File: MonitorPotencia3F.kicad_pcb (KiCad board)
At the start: 2 copper layers, 95.9 x 97.2 mm, 42 parts, among them J1 Conn_01x02, J2 Conn_01x02, J3 Conn_01x02, J4 Conn_01x02, J5 Conn_01x02, J6 Conn_01x04, J7 Conn_01x04, J8 Conn_01x04, J9 Conn_02x09_Odd_Even, U1 LM7805, U2 ESP32-DEVKIT-V1, U3 LM324

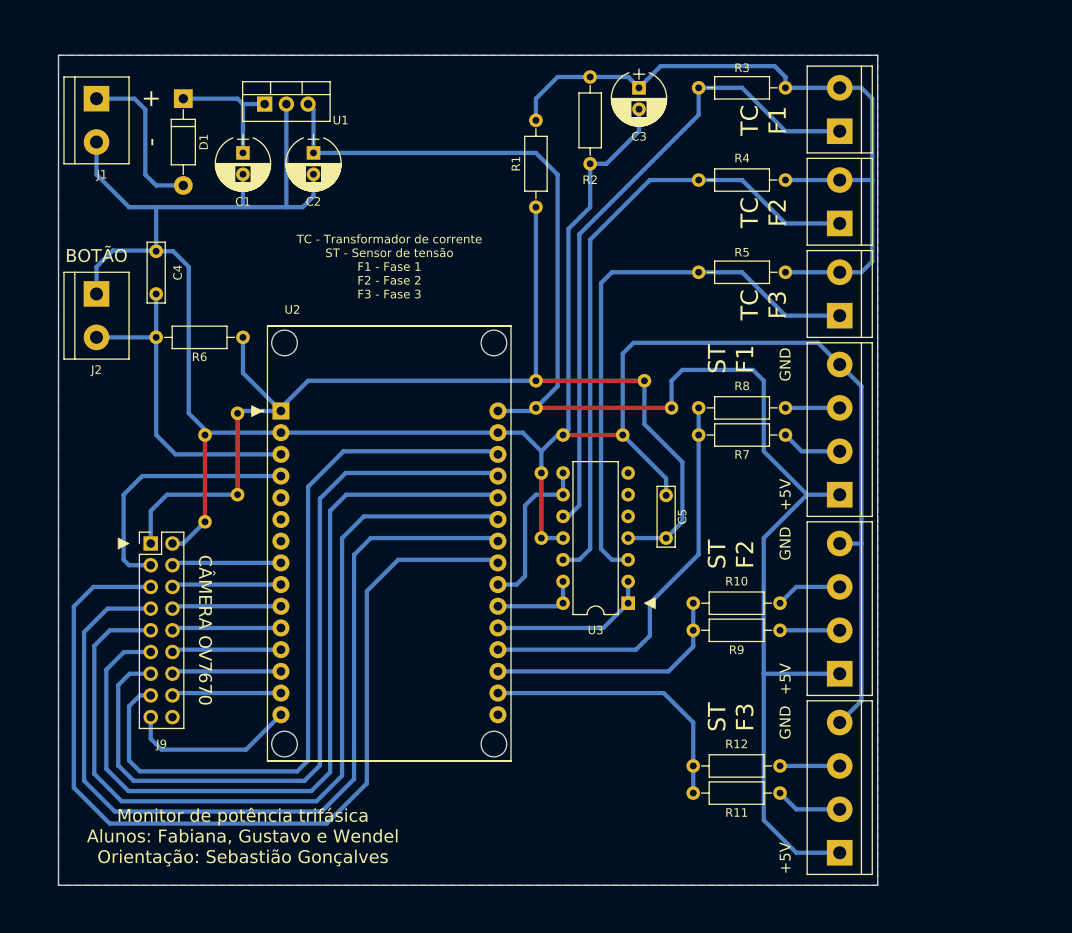
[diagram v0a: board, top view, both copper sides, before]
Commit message: PCB e modelo 3D foram completados. As alterações necessárias foram feitas no esquemático para refletir o projeto desenvolvido na PCB. Teve-se que alterar o modelo do ESP32 para aquele que foi adquirido para o projeto.
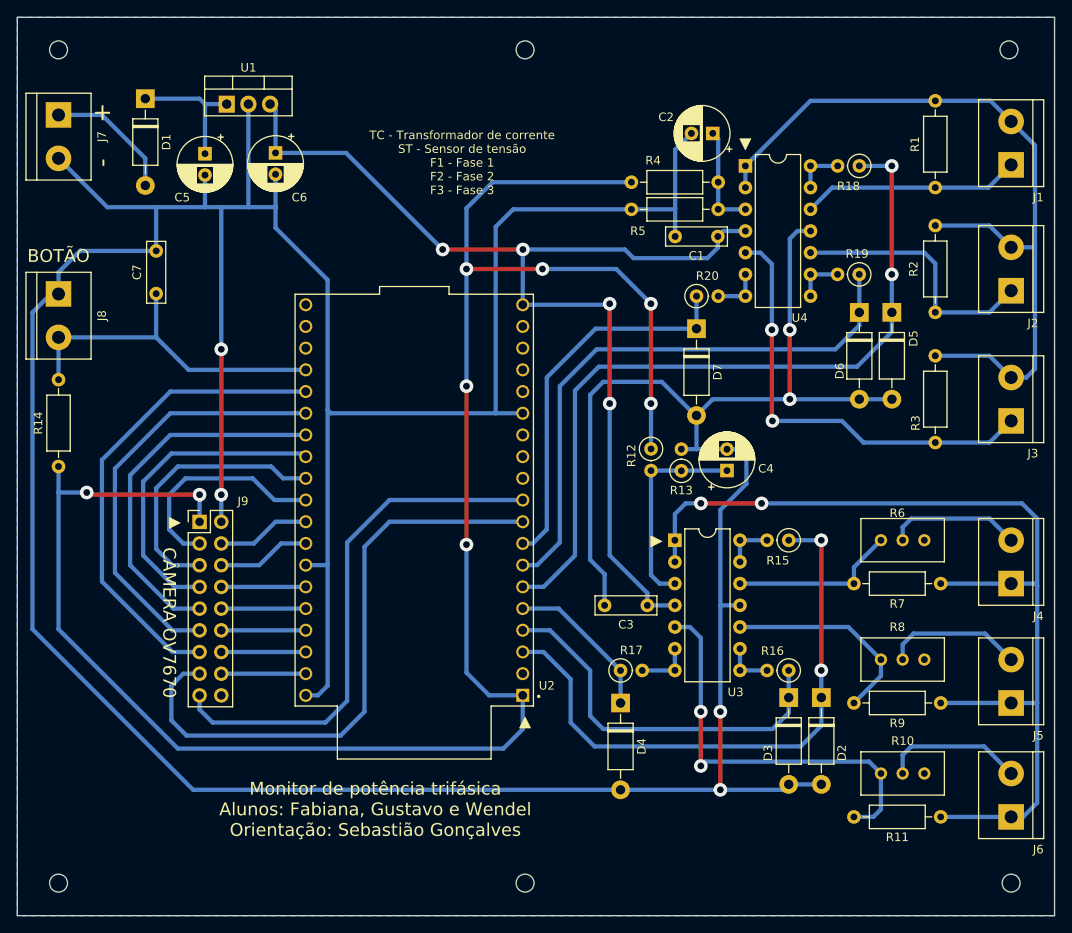
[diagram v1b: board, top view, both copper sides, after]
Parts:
- removed the REF** at (161.3, 82.5)
- removed the REF** at (122.6, 95.9)
- removed the REF** at (161.9, 90.2)
- removed the REF** at (122.6, 85.7)
- removed the REF** at (161.9, 97.8)
- removed the REF** at (161.3, 79.4)
- removed the REF** at (126.4, 92.7)
- removed the REF** at (174.0, 79.4)
- removed the REF** at (171.4, 85.7)
- removed the REF** at (177.2, 82.5)
- removed the REF** at (126.4, 83.2)
- removed the REF** at (164.5, 85.7)
- added C6: 100uF, Capacitor_THT:CP_Radial_D6.3mm_P2.50mm, F.Cu at (130.8, 52.7)
- added C7: 100nF, Capacitor_THT:C_Rect_L7.0mm_W2.0mm_P5.00mm, F.Cu at (116.8, 69.2)
- added D2: 1N4728A, Diode_THT:D_DO-41_SOD81_P10.16mm_Horizontal, F.Cu at (194.7, 116.5)
- added D3: 1N4728A, Diode_THT:D_DO-41_SOD81_P10.16mm_Horizontal, F.Cu at (190.9, 116.5)
- added D4: 1N4728A, Diode_THT:D_DO-41_SOD81_P10.16mm_Horizontal, F.Cu at (171.2, 117.1)
- added D5: 1N4728A, Diode_THT:D_DO-41_SOD81_P10.16mm_Horizontal, F.Cu at (203.0, 71.4)
- added D6: 1N4728A, Diode_THT:D_DO-41_SOD81_P10.16mm_Horizontal, F.Cu at (199.1, 71.4)
- added D7: 1N4728A, Diode_THT:D_DO-41_SOD81_P10.16mm_Horizontal, F.Cu at (180.1, 73.3)
- added R13: 10K, Resistor_THT:R_Axial_DIN0207_L6.3mm_D2.5mm_P2.54mm_Vertical, F.Cu at (178.3, 89.9)
- added R14: 4k7, Resistor_THT:R_Axial_DIN0207_L6.3mm_D2.5mm_P10.16mm_Horizontal, F.Cu at (105.4, 89.4)
- added R15: 10R, Resistor_THT:R_Axial_DIN0207_L6.3mm_D2.5mm_P2.54mm_Vertical, F.Cu at (190.9, 98.0)
- added R16: 10R, Resistor_THT:R_Axial_DIN0207_L6.3mm_D2.5mm_P2.54mm_Vertical, F.Cu at (190.9, 113.3)
- added R17: 10R, Resistor_THT:R_Axial_DIN0207_L6.3mm_D2.5mm_P2.54mm_Vertical, F.Cu at (171.2, 113.3)
- added R18: 10R, Resistor_THT:R_Axial_DIN0207_L6.3mm_D2.5mm_P2.54mm_Vertical, F.Cu at (199.1, 54.2)
- added R19: 10R, Resistor_THT:R_Axial_DIN0207_L6.3mm_D2.5mm_P2.54mm_Vertical, F.Cu at (199.1, 66.9)
- added R20: 10R, Resistor_THT:R_Axial_DIN0207_L6.3mm_D2.5mm_P2.54mm_Vertical, F.Cu at (180.1, 69.5)
- added REF**: MountingHole_2.1mm, MountingHole:MountingHole_2.1mm, F.Cu at (160.0, 40.6)
- added REF**: MountingHole_2.1mm, MountingHole:MountingHole_2.1mm, F.Cu at (160.0, 138.2)
- added REF**: MountingHole_2.1mm, MountingHole:MountingHole_2.1mm, F.Cu at (105.4, 40.6)
- added REF**: MountingHole_2.1mm, MountingHole:MountingHole_2.1mm, F.Cu at (216.9, 138.2)
- added REF**: MountingHole_2.1mm, MountingHole:MountingHole_2.1mm, F.Cu at (105.4, 138.2)
- added REF**: MountingHole_2.1mm, MountingHole:MountingHole_2.1mm, F.Cu at (216.7, 40.6)
- added U4: LM324, Package_DIP:DIP-14_W7.62mm, F.Cu at (185.8, 54.2)
- C1: value 100uF -> 100nF; footprint Capacitors_THT:CP_Radial_D6.3mm_P2.50mm -> Capacitor_THT:C_Rect_L7.0mm_W2.0mm_P5.00mm
- C2: value 100uF -> 1uF; footprint Capacitors_THT:CP_Radial_D6.3mm_P2.50mm -> Capacitor_THT:CP_Radial_D6.3mm_P2.50mm
- C3: value 1uF -> 100nF; footprint Capacitors_THT:CP_Radial_D6.3mm_P2.50mm -> Capacitor_THT:C_Rect_L7.0mm_W2.0mm_P5.00mm
- C4: value 100nF -> 1uF; footprint Capacitors_THT:C_Rect_L7.0mm_W2.0mm_P5.00mm -> Capacitor_THT:CP_Radial_D6.3mm_P2.50mm
- C5: value 100nF -> 100uF; footprint Capacitors_THT:C_Rect_L7.0mm_W2.0mm_P5.00mm -> Capacitor_THT:CP_Radial_D6.3mm_P2.50mm
- D1: footprint Diodes_THT:D_DO-41_SOD81_P10.16mm_Horizontal -> Diode_THT:D_DO-41_SOD81_P10.16mm_Horizontal
- J1, J2, J3, J4, J5: footprint Connectors_Terminal_Blocks:TerminalBlock_bornier-2_P5.08mm -> TerminalBlock:TerminalBlock_bornier-2_P5.08mm
- J6, J7, J8: value Conn_01x04 -> Conn_01x02; footprint Connectors_Terminal_Blocks:TerminalBlock_bornier-4_P5.08mm -> TerminalBlock:TerminalBlock_bornier-2_P5.08mm
- J9: footprint Pin_Headers:Pin_Header_Straight_2x09_Pitch2.54mm -> Connector_PinHeader_2.54mm:PinHeader_2x09_P2.54mm_Vertical
- R1, R2: value 10k -> 22; footprint Resistors_THT:R_Axial_DIN0207_L6.3mm_D2.5mm_P10.16mm_Horizontal -> Resistor_THT:R_Axial_DIN0207_L6.3mm_D2.5mm_P10.16mm_Horizontal
- R10, R8: value 10k -> 100k; footprint Resistors_THT:R_Axial_DIN0207_L6.3mm_D2.5mm_P10.16mm_Horizontal -> Potentiometer_THT:Potentiometer_Bourns_3296W_Vertical
- R11, R7, R9: value 1k -> 10k; footprint Resistors_THT:R_Axial_DIN0207_L6.3mm_D2.5mm_P10.16mm_Horizontal -> Resistor_THT:R_Axial_DIN0207_L6.3mm_D2.5mm_P10.16mm_Horizontal
- R12: value 10k -> 10K; footprint Resistors_THT:R_Axial_DIN0207_L6.3mm_D2.5mm_P10.16mm_Horizontal -> Resistor_THT:R_Axial_DIN0207_L6.3mm_D2.5mm_P2.54mm_Vertical
- R3: footprint Resistors_THT:R_Axial_DIN0207_L6.3mm_D2.5mm_P10.16mm_Horizontal -> Resistor_THT:R_Axial_DIN0207_L6.3mm_D2.5mm_P10.16mm_Horizontal
- R4, R5: value 22 -> 10k; footprint Resistors_THT:R_Axial_DIN0207_L6.3mm_D2.5mm_P10.16mm_Horizontal -> Resistor_THT:R_Axial_DIN0207_L6.3mm_D2.5mm_P10.16mm_Horizontal
- R6: value 4k7 -> 100k; footprint Resistors_THT:R_Axial_DIN0207_L6.3mm_D2.5mm_P10.16mm_Horizontal -> Potentiometer_THT:Potentiometer_Bourns_3296W_Vertical
- U1: footprint TO_SOT_Packages_THT:TO-220-3_Vertical -> Package_TO_SOT_THT:TO-220-3_Vertical
- U2: value ESP32-DEVKIT-V1 -> ESP32-DEVKITC; footprint ESP32-DEVKIT-V1:MODULE_ESP32_DEVKIT_V1 -> ESP32-DEVKITC:MODULE_ESP32-DEVKITC
- U3: footprint Housings_DIP:DIP-14_W7.62mm -> Package_DIP:DIP-14_W7.62mm
- moved J7 112.4 mm to (105.4, 48.3), turned to -90 degrees
- moved J8 112.4 mm to (105.4, 69.2), turned to -90 degrees
- moved J1 107.3 mm to (216.9, 54.1), turned to 90 degrees
- moved J2 107.1 mm to (216.9, 68.8), turned to 90 degrees
- moved R6 78.4 mm to (201.7, 98.0)
- moved C5 70.3 mm to (122.6, 52.8), turned to -90 degrees
- moved C4 69.9 mm to (183.7, 89.9)
- moved C3 60.6 mm to (174.3, 105.7), turned to 180 degrees
- moved C1 56.4 mm to (182.6, 62.5), turned to 180 degrees
- moved R3 49.9 mm to (208.0, 86.6), turned to 90 degrees
- moved J5 49.6 mm to (216.9, 117.1)
- moved R1 46.8 mm to (208.0, 56.8)
- moved C2 46.8 mm to (182.0, 50.4), turned to 180 degrees
- moved J4 46.7 mm to (216.9, 103.1)
- moved R2 44.0 mm to (208.0, 61.2)
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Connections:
- C1 pad 1: Net-(C1-Pad1) -> +5V
- C2 pad 1: +5V -> Net-(C2-Pad1)
- C3 pad 1: SEN_CORR_REF -> +5V
- C4 pad 1: BOTAO -> Net-(C4-Pad1)
- C5 pad 1: +3V3 -> Net-(C5-Pad1)
- D1 pad 1: Net-(C1-Pad1) -> Net-(C5-Pad1)
- J1 pad 1: Net-(D1-Pad2) -> Net-(J1-Pad1)
- J1 pad 2: GND -> SEN_CORR_REF
- J2 pad 1: GND -> Net-(J2-Pad1)
- J2 pad 2: BOTAO -> SEN_CORR_REF
- J4 pad 1: Net-(J4-Pad1) -> SEN_TENSAO_REF
- J4 pad 2: SEN_CORR_REF -> Net-(J4-Pad2)
- J5 pad 1: Net-(J5-Pad1) -> SEN_TENSAO_REF
- J5 pad 2: SEN_CORR_REF -> Net-(J5-Pad2)
- J6 pad 1: +5V -> SEN_TENSAO_REF
- J7 pad 1: +5V -> Net-(D1-Pad2)
- J7 pad 2: Net-(J7-Pad2) -> GND
- J8 pad 1: +5V -> GND
- J8 pad 2: Net-(J8-Pad2) -> BOTAO
- J9 pad 18: (no net) -> unconnected-(J9-Pad18)
- R1 pad 1: +3V3 -> Net-(J1-Pad1)
- R10 pad 1: Net-(J7-Pad3) -> Net-(R10-Pad1)
- R10 pad 2: SENS_TENSAO_F2 -> Net-(J6-Pad2)
- R11 pad 1: Net-(J8-Pad2) -> SEN_TENSAO_REF
- R11 pad 2: SENS_TENSAO_F3 -> Net-(R10-Pad1)
- R12 pad 1: Net-(J8-Pad3) -> +3V3
- R12 pad 2: SENS_TENSAO_F3 -> Net-(C4-Pad1)
- R2 pad 2: GND -> Net-(J2-Pad1)
- R4 pad 1: SEN_CORR_REF -> +3V3
- R4 pad 2: Net-(J4-Pad1) -> Net-(C2-Pad1)
- R5 pad 1: Net-(J5-Pad1) -> Net-(C2-Pad1)
- R5 pad 2: SEN_CORR_REF -> GND
- R6 pad 1: +3V3 -> Net-(R6-Pad1)
- R6 pad 2: BOTAO -> Net-(J4-Pad2)
- R7 pad 1: Net-(J6-Pad2) -> SEN_TENSAO_REF
- R7 pad 2: SENS_TENSAO_F1 -> Net-(R6-Pad1)
- R8 pad 1: Net-(J6-Pad3) -> Net-(R8-Pad1)
- R8 pad 2: SENS_TENSAO_F1 -> Net-(J5-Pad2)
- R9 pad 1: Net-(J7-Pad2) -> SEN_TENSAO_REF
- R9 pad 2: SENS_TENSAO_F2 -> Net-(R8-Pad1)
- U1 pad 1: Net-(C1-Pad1) -> Net-(C5-Pad1)
- U2 pad 10: XCLK -> RESET
- U2 pad 11: D6 -> unconnected-(U2-Pad11)
- U2 pad 12: D4 -> unconnected-(U2-Pad12)
- U2 pad 13: D2 -> unconnected-(U2-Pad13)
- U2 pad 14: D0 -> GND
- U2 pad 15: RESET -> unconnected-(U2-Pad15)
- U2 pad 16: (no net) -> unconnected-(U2-Pad16)
- U2 pad 17: SENS_TENSAO_F3 -> unconnected-(U2-Pad17)
- U2 pad 18: SENS_TENSAO_F2 -> unconnected-(U2-Pad18)
- U2 pad 19: SENS_TENSAO_F1 -> +5V
- U2 pad 2: GND -> unconnected-(U2-Pad2)
- U2 pad 20: SENS_CORR_F3 -> unconnected-(U2-Pad20)
- U2 pad 21: SENS_CORR_F2 -> unconnected-(U2-Pad21)
- U2 pad 22: SENS_CORR_F1 -> unconnected-(U2-Pad22)
- U2 pad 23: VSYNC -> BOTAO
- U2 pad 24: PCLK -> D3
- U2 pad 25: D7 -> D5
- U2 pad 26: D5 -> D7
- U2 pad 27: D3 -> PCLK
- U2 pad 28: D1 -> VSYNC
- U2 pad 29: GND -> SIOC
- U2 pad 3: BOTAO -> /CircuitoDigital/SENS_TENSAO_F1
- U2 pad 30: +5V -> SIOD
- U2 pad 4: SIOC -> /CircuitoDigital/SENS_TENSAO_F2
- U2 pad 5: (no net) -> /CircuitoDigital/SENS_TENSAO_F3
- U2 pad 6: (no net) -> /CircuitoDigital/SENS_CORR_F1
- U2 pad 7: (no net) -> /CircuitoDigital/SENS_CORR_F2
- U2 pad 8: SIOD -> /CircuitoDigital/SENS_CORR_F3
- U2 pad 9: HREF -> D1
- U3 pad 1: SENS_CORR_F3 -> SEN_TENSAO_REF
- U3 pad 10: Net-(J3-Pad1) -> Net-(R8-Pad1)
- U3 pad 12: Net-(J4-Pad1) -> Net-(R6-Pad1)
- U3 pad 13: SENS_CORR_F2 -> Net-(R15-Pad2)
- U3 pad 14: SENS_CORR_F2 -> Net-(R15-Pad2)
- U3 pad 2: SENS_CORR_F3 -> SEN_TENSAO_REF
- U3 pad 3: Net-(J5-Pad1) -> Net-(C4-Pad1)
- U3 pad 4: +3V3 -> +5V
- U3 pad 5: (no net) -> Net-(R10-Pad1)
- U3 pad 6: (no net) -> Net-(R17-Pad2)
- U3 pad 7: (no net) -> Net-(R17-Pad2)
- U3 pad 8: SENS_CORR_F1 -> Net-(R16-Pad2)
- U3 pad 9: SENS_CORR_F1 -> Net-(R16-Pad2)
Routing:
- net GND: track 304.5 -> 529.5 mm, vias 0 -> 6
- net SEN_TENSAO_REF: track 0.00 -> 117.2 mm, vias 0 -> 2
- net +3V3: track 130.0 -> 226.7 mm, vias 0 -> 8
- net /CircuitoDigital/SENS_CORR_F1: track 0.00 -> 90.1 mm, vias 0 -> 2
- net VSYNC: track 108.9 -> 32.1 mm
- net Net-(J4-Pad1): track 74.1 -> 0.00 mm
- net /CircuitoDigital/SENS_TENSAO_F1: track 0.00 -> 69.0 mm, vias 0 -> 2
- net PCLK: track 105.3 -> 37.3 mm
- net /CircuitoDigital/SENS_CORR_F2: track 0.00 -> 67.7 mm
- net Net-(J5-Pad1): track 65.4 -> 0.00 mm
- net D7: track 101.4 -> 43.3 mm
- net +5V: track 178.3 -> 125.2 mm, vias 0 -> 4
- net Net-(R10-Pad1): track 0.00 -> 48.1 mm, vias 0 -> 2
- net SENS_TENSAO_F1: track 47.5 -> 0.00 mm
- net D5: track 97.2 -> 49.9 mm
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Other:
- board size 95.9 x 97.2 mm -> 121.4 x 105.2 mm
- board text removed: "+5V"
- board text removed: "GND"
- board text removed: "ST F1"
- board text removed: "ST F2"
- board text removed: "ST F3"
- board text removed: "TC F1"
- board text removed: "TC F2"
- board text removed: "TC F3"
